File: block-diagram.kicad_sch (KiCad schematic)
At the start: 0 parts

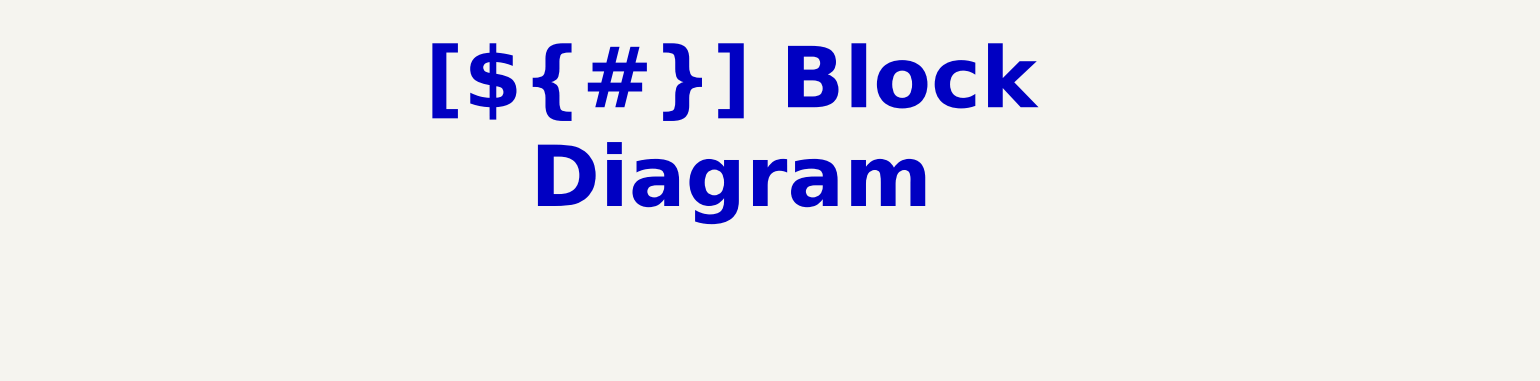
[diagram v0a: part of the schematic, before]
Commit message: feat: convert template to Boardwright
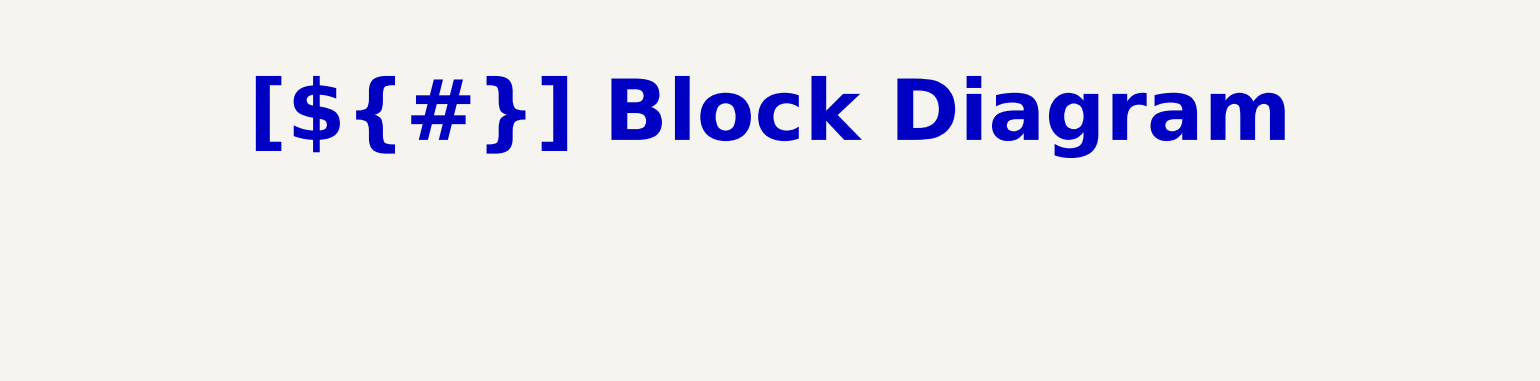
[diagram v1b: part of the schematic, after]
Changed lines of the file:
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@@
 	(text_box "[${#}] ${TITLE}"
 		(exclude_from_sim no)
-		(at 144.78 15 0)
-		(size 130.81 15)
+		(at 20.32 10.16 0)
+		(size 389.89 20.32)
 		(margins 5.9999 5.9999 5.9999 5.9999)
 		(stroke
